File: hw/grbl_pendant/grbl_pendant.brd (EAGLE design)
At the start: 100 x 100 mm, 30 parts, among them CON1 MOLEX-53261-0671, IC2 FT232RL, Q1 14.7456 MHz, X1 PN61729-S

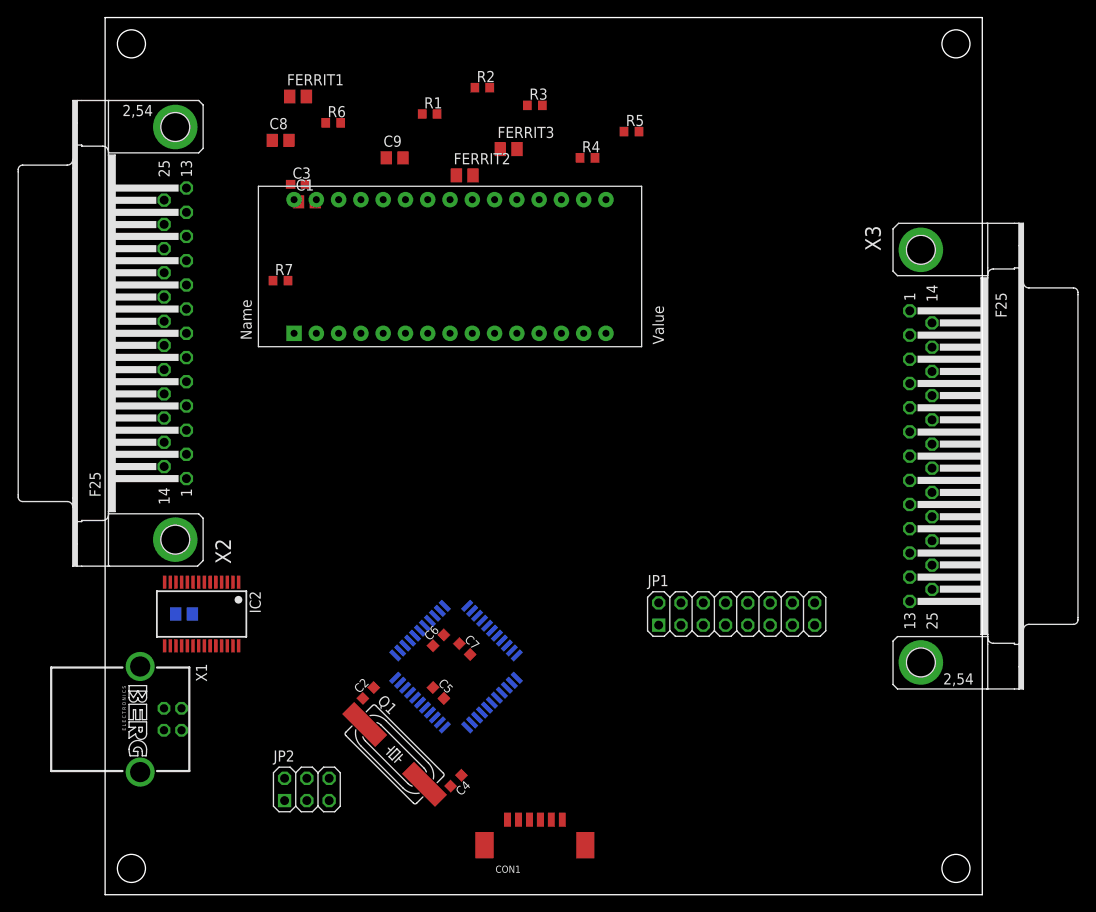
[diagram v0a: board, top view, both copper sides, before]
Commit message: grbl_pendant_peripheral v1 layout
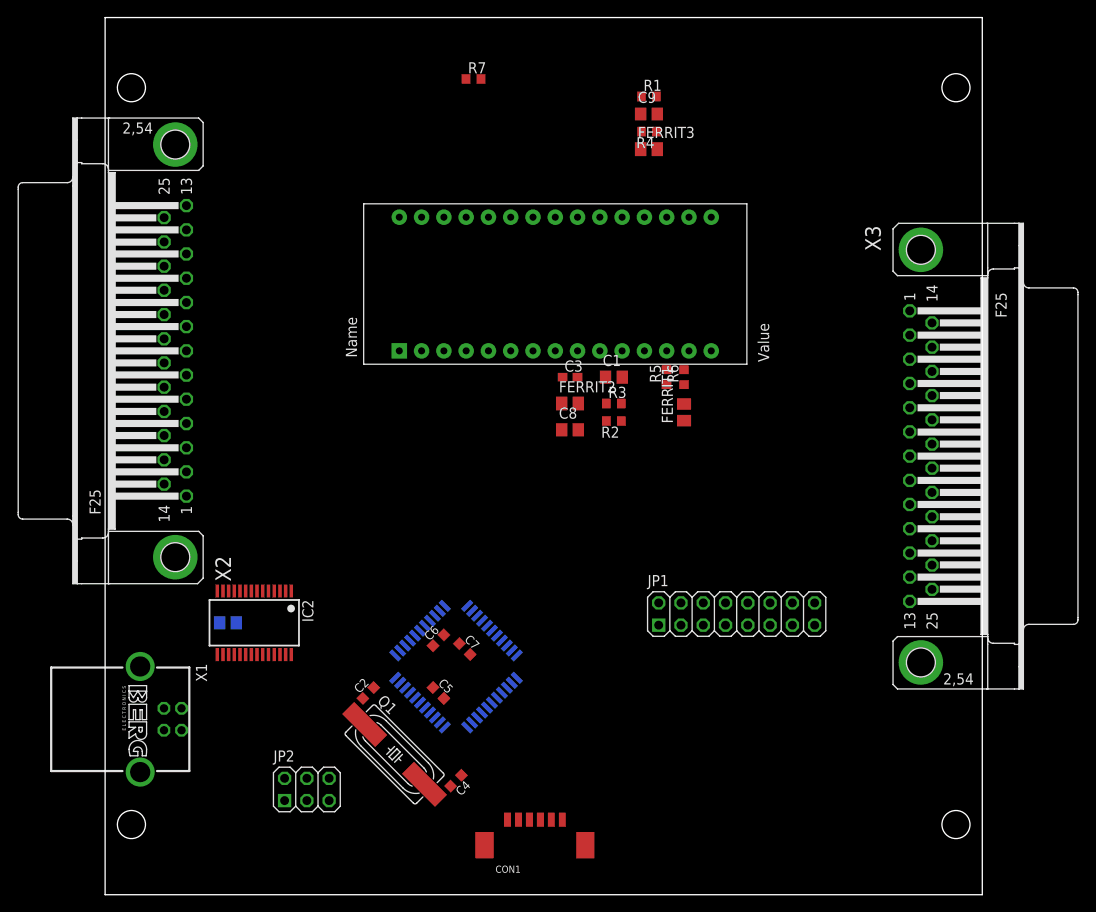
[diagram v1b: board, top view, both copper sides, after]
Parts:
- moved FERRIT1 56.9 mm to (66.0, 55.0), turned to 90 degrees
- moved R6 49.4 mm to (66.0, 59.0), turned to 90 degrees
- moved C8 46.7 mm to (53.0, 53.0)
- moved R2 40.9 mm to (58.0, 54.0), turned to 180 degrees
- moved C1 40.3 mm to (58.0, 59.0)
- moved C3 38.0 mm to (53.0, 59.0)
- moved R3 35.2 mm to (58.0, 56.0)
- moved R7 31.8 mm to (42.0, 93.0)
- moved C9 29.4 mm to (62.0, 89.0)
- moved FERRIT2 28.6 mm to (53.0, 56.0)
- moved R5 28.3 mm to (64.0, 59.0), turned to 90 degrees
- moved R1 25.1 mm to (62.0, 91.0)
- moved FERRIT3 16.0 mm to (62.0, 85.0)
- moved U$2 12.2 mm to (31.0, 62.0)
- moved R4 7.62 mm to (62.0, 87.0), turned to 180 degrees
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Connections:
- net LED_SHIFT_RCK: no longer X3.23
- net LED_SHIFT_SCK: now also X3.23

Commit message: main board and pendant finished layouts
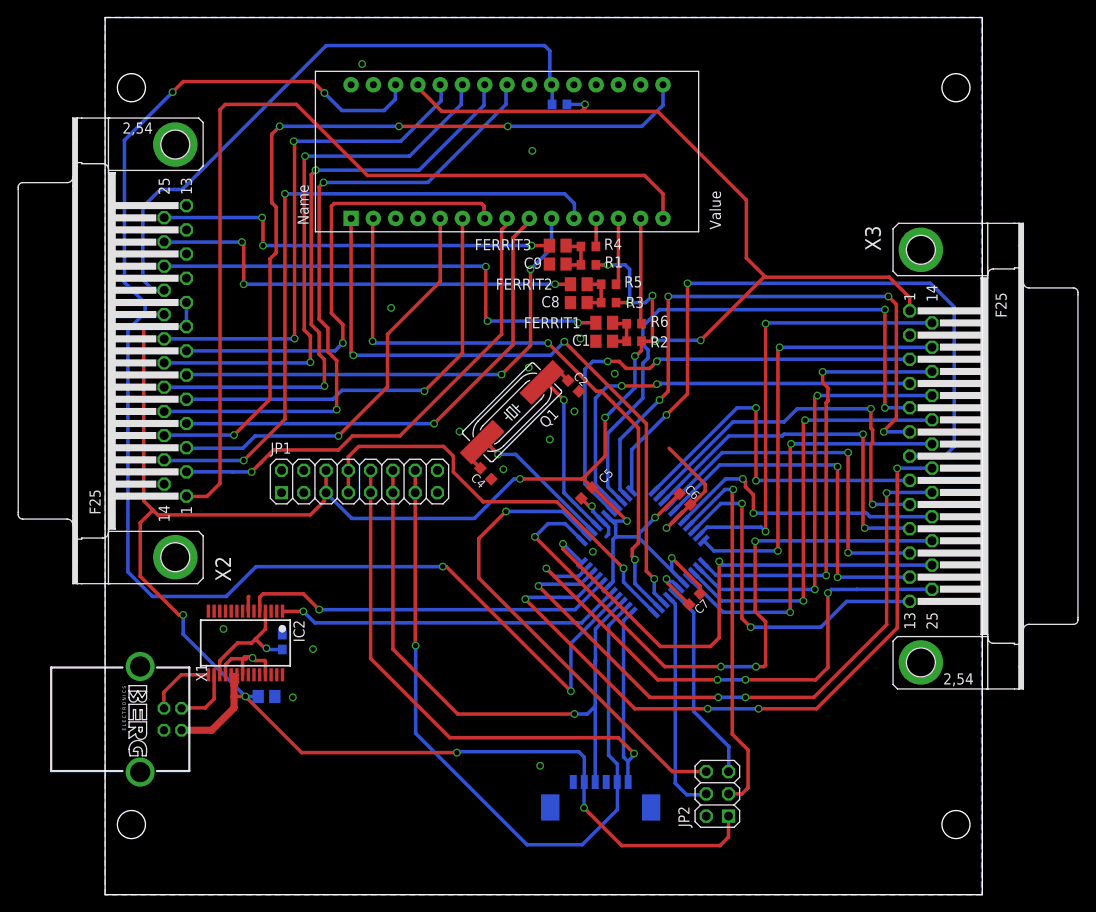
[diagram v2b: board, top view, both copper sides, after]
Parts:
- removed U$1: MEGA162MA*A*, avr-7:TQFP44
- added IC1: MEGA162MA*A*, avr-7:TQFP44
- moved JP2 46.8 mm to (69.8, 11.5), turned to 90 degrees
- moved JP1 45.6 mm to (29.0, 47.1)
- moved C3 44.6 mm to (20.2, 28.8), flipped to the bottom, turned to 270 degrees
- moved C2 42.1 mm to (53.4, 58.0), turned to 315 degrees
- moved Q1 41.2 mm to (46.4, 55.0), turned to 225 degrees
- moved C4 35.2 mm to (43.4, 48.0), turned to 135 degrees
- moved C6 32.4 mm to (66.1, 45.1), turned to 315 degrees
- moved C5 28.4 mm to (54.9, 45.8), turned to 225 degrees
- moved C7 26.8 mm to (67.2, 33.7), turned to 225 degrees
- moved R1 20.4 mm to (55.1, 71.8), turned to 180 degrees
- moved C9 20.0 mm to (51.6, 71.9)
- moved U$2 16.1 mm to (25.5, 77.1)
- moved FERRIT3 15.1 mm to (51.6, 74.0)
- moved R4 14.8 mm to (55.1, 73.9), turned to 0 degrees
- moved C8 14.5 mm to (54.0, 67.5)
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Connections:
- net +5V: now also IC1.17, IC1.38, IC1.6; no longer U$1.17, U$1.38, U$1.6
- net BTN1: now also IC1.37; no longer U$1.37
- net BTN2: now also IC1.36; no longer U$1.36
- net BTN3: now also IC1.35; no longer U$1.35
- net BTN4: now also IC1.34; no longer U$1.34
- net BTN5: now also IC1.33; no longer U$1.33
- net BTN6: now also IC1.32; no longer U$1.32
- net BTN_JOG: now also IC1.31; no longer U$1.31
- net DISP_D0: now also IC1.18; no longer U$1.18
- net DISP_D1: now also IC1.19; no longer U$1.19
- net DISP_D2: now also IC1.20; no longer U$1.20
- net DISP_D3: now also IC1.21; no longer U$1.21
- net DISP_D4: now also IC1.22; no longer U$1.22
- net DISP_D5: now also IC1.23; no longer U$1.23
- net DISP_D6: now also IC1.24; no longer U$1.24
- net DISP_D7: now also IC1.25; no longer U$1.25
- net DISP_ENABLE: now also IC1.27; no longer U$1.27
- net DISP_RS: now also IC1.26; no longer U$1.26
- net ENCODER_A: now also IC1.8; no longer U$1.8
- net ENCODER_B: now also IC1.9; no longer U$1.9
- net ENCODER_BTN: now also IC1.29; no longer U$1.29
- net GND: now also IC1.16, IC1.28, IC1.39; no longer U$1.16, U$1.28, U$1.39
- net LED_SHIFT_RCK: now also IC1.11; no longer U$1.11
- net LED_SHIFT_SCK: now also IC1.12; no longer U$1.12
- net LED_SHIFT_SI: now also IC1.10; no longer U$1.10
- net MISO: now also IC1.2; no longer U$1.2
- net MOSI: now also IC1.1; no longer U$1.1
- net N$7: now also IC1.14; no longer U$1.14
- net N$8: now also IC1.15; no longer U$1.15
- net RESET_AVR: now also IC1.4; no longer U$1.4
- net RXD_BRIDGE: now also IC1.42; no longer U$1.42
- net RXD_PC: now also IC1.7; no longer U$1.7
- net SCK: now also IC1.3; no longer U$1.3
- net SD_IO_1: now also IC1.30; no longer U$1.30
- net SD_IO_2: now also IC1.41; no longer U$1.41
- net SD_IO_3: now also IC1.40; no longer U$1.40
- net SD_IO_4: now also IC1.13; no longer U$1.13
- net SS: now also IC1.44; no longer U$1.44
- net TXD_BRIDGE: now also IC1.43; no longer U$1.43
- net TXD_PC: now also IC1.5; no longer U$1.5
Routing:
- net +5V: track 0.00 -> 369.9 mm, vias 0 -> 16
- net RESET_AVR: track 0.00 -> 162.4 mm, vias 0 -> 4
- net SPINDLE_ENABLE: track 0.00 -> 104.8 mm
- net SPINDLE_DIR: track 0.00 -> 93.1 mm, vias 0 -> 4
- net MISO: track 0.00 -> 84.2 mm, vias 0 -> 1
- net ENCODER_A: track 0.00 -> 82.9 mm, vias 0 -> 4
- net DISP_D4: track 0.00 -> 79.3 mm, vias 0 -> 2
- net MOSI: track 0.00 -> 77.1 mm, vias 0 -> 1
- net STEPPER_DISABLE: track 0.00 -> 76.6 mm, vias 0 -> 2
- net ENCODER_B: track 0.00 -> 75.3 mm, vias 0 -> 4
- net RXD_BRIDGE: track 0.00 -> 74.9 mm, vias 0 -> 3
- net LED_SHIFT_SCK: track 0.00 -> 74.3 mm, vias 0 -> 4
- net COOLING_ENABLE: track 0.00 -> 73.5 mm, vias 0 -> 2
- net Z_PROBE: track 0.00 -> 71.7 mm
- net TXD_BRIDGE: track 0.00 -> 70.4 mm, vias 0 -> 3
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- added copper zone on layer 1, net GND
- added copper zone on layer 16, net GND
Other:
- board text added: "GRBL Board V4 with Pendant Armin Schlegel 07.09.2015"
